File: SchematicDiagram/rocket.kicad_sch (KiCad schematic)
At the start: 5 parts, among them SW1 SW_Push, U1 ESP32-DevKitC

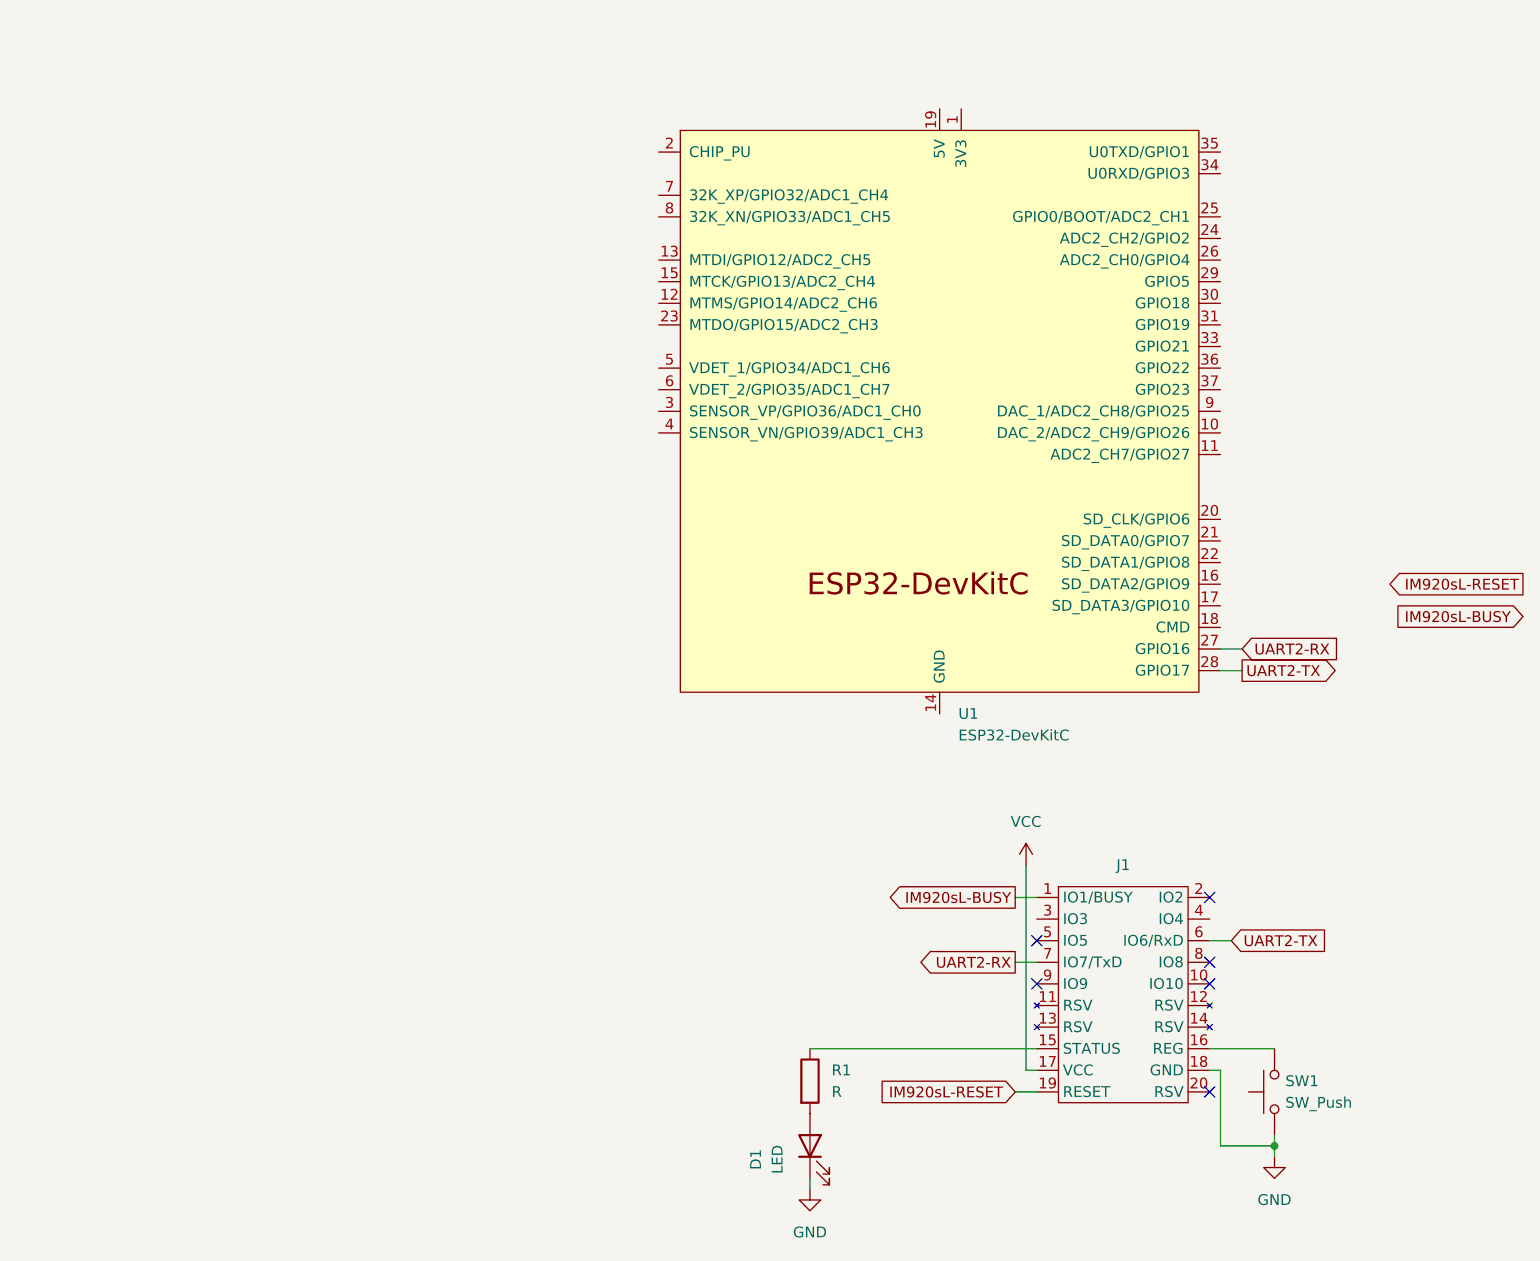
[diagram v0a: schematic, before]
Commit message: add symbole of Regulator Linear
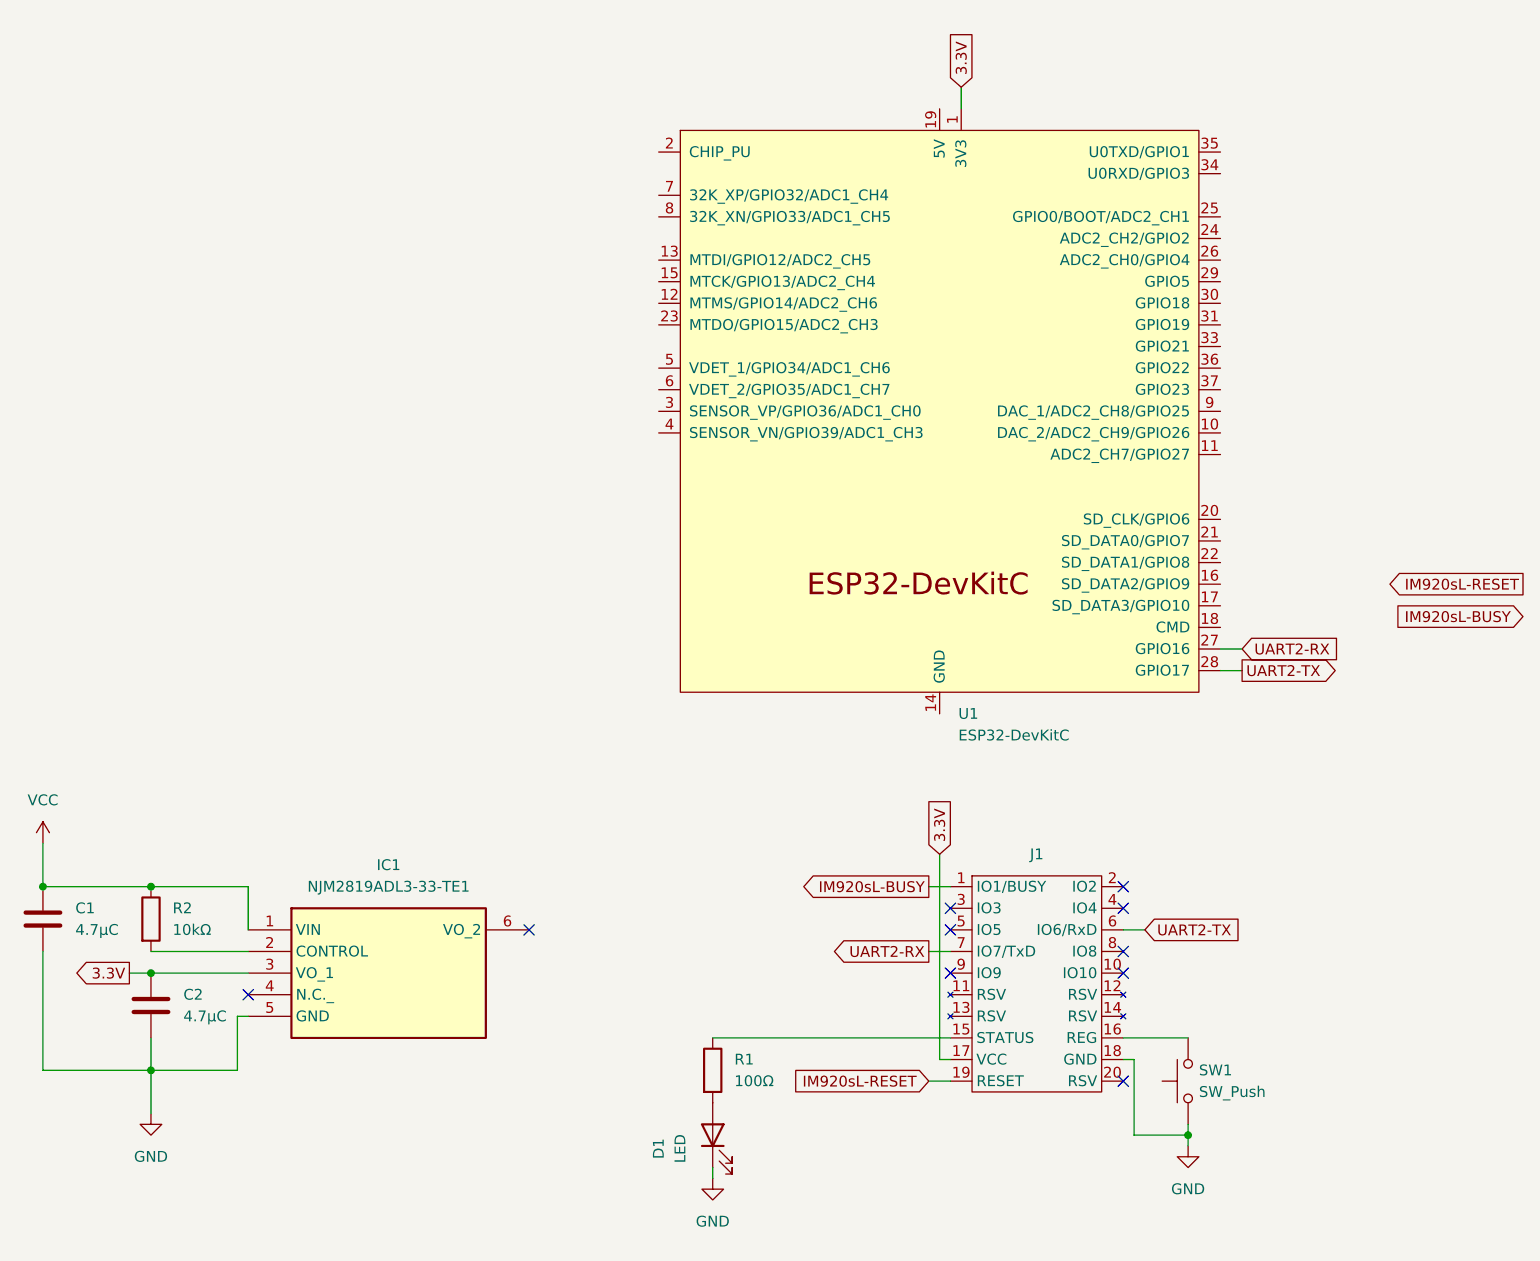
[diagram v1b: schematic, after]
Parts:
- added C1, C2: 4.7μC, symbol Device:C
- added IC1: NJM2819ADL3-33-TE1, NJM2819ADL333TE1, symbol NJM2819ADL3-33-TE1:NJM2819ADL3-33-TE1
- added R2: 10kΩ, symbol Device:R
- R1: value R -> 100Ω
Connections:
- net GND: now also C1.1, C2.1, IC1.5 (GND)
- net VCC: now also C1.2, IC1.1 (VIN), R2.1; no longer J1.17 (VCC)
- net 3.3V: now reaches U1.1 (3V3)
- net 3.3V: now also J1.17 (VCC), C2.2, IC1.3 (VO_1)
- new net: IC1.2 (CONTROL), R2.2
- no-connect marks 6 -> 10
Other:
- moved on the sheet: D1, J1, R1, SW1

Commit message: self voltage manegment
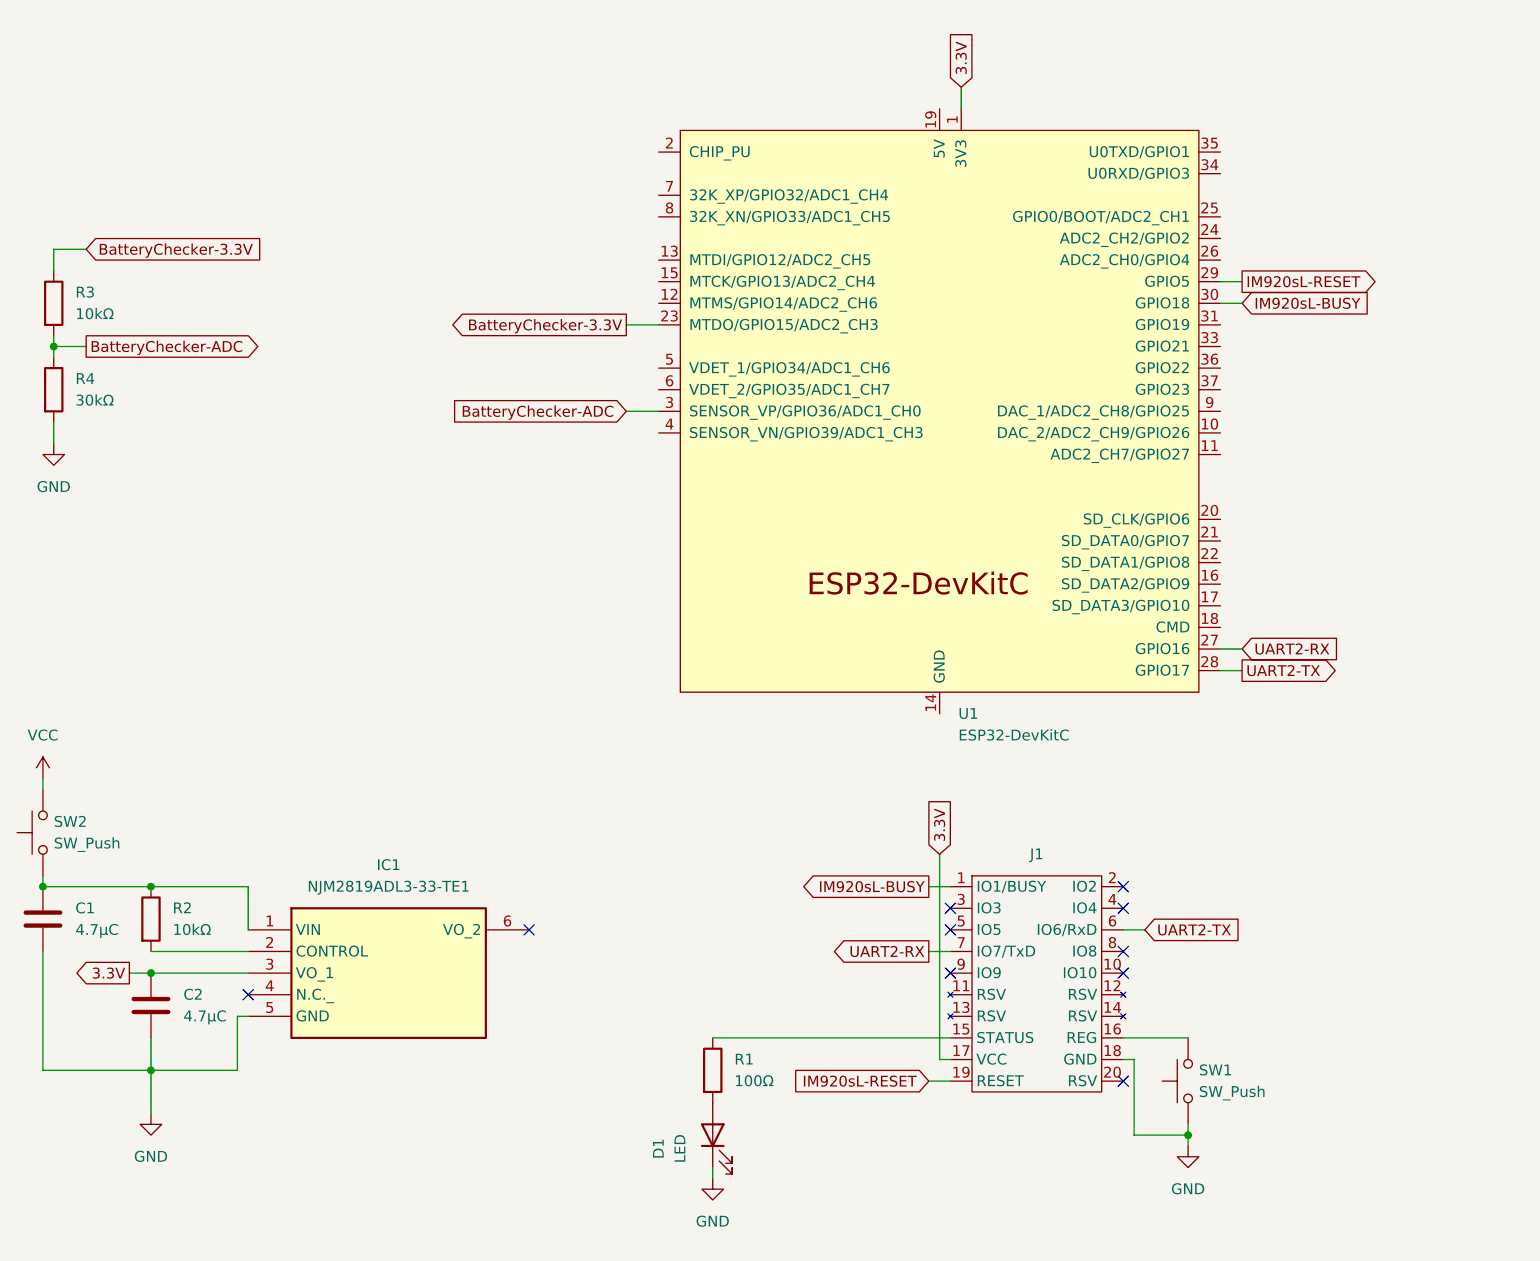
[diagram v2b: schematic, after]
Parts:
- added R3: 10kΩ, symbol Device:R
- added R4: 30kΩ, symbol Device:R
- added SW2: SW_Push, symbol Switch:SW_Push
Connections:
- net GND: now also R4.2
- net IM920sL-BUSY: now also U1.30 (GPIO18)
- net IM920sL-RESET: now also U1.29 (GPIO5)
- net VCC: now also SW2.2; no longer C1.2, IC1.1 (VIN), R2.1
- net BatteryChecker-3.3V: now reaches U1.23 (MTDO/GPIO15/ADC2_CH3)
- net BatteryChecker-3.3V: now also R3.1
- net BatteryChecker-ADC: now reaches U1.3 (SENSOR_VP/GPIO36/ADC1_CH0)
- net BatteryChecker-ADC: now also R3.2, R4.1
- new net: C1.2, IC1.1 (VIN), R2.1, SW2.1
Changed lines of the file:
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@@
   (junction (at 120.65 120.65) (diameter 0) (color 0 0 0 0)
+  )
+  (junction (at 109.22 57.15) (diameter 0) (color 0 0 0 0)
   )
   (junction (at 120.65 130.81) (diameter 0) (color 0 0 0 0)
@@
     (stroke (width 0) (type default))
   )
+  (wire (pts (xy 109.22 68.58) (xy 109.22 66.04))
+    (stroke (width 0) (type default))
+  )
+  (wire (pts (xy 176.53 54.61) (xy 180.34 54.61))
+    (stroke (width 0) (type default))
+  )
   (wire (pts (xy 236.22 149.86) (xy 242.57 149.86))
     (stroke (width 0) (type default))
@@
     (stroke (width 0) (type default))
   )
+  (wire (pts (xy 248.92 52.07) (xy 246.38 52.07))
+    (stroke (width 0) (type default))
+  )
   (wire (pts (xy 118.11 130.81) (xy 120.65 130.81))
     (stroke (width 0) (type default))
   )
+  (wire (pts (xy 107.95 109.22) (xy 107.95 107.95))
+    (stroke (width 0) (type default))
+  )
   (wire (pts (xy 212.09 143.51) (xy 214.63 143.51))
     (stroke (width 0) (type default))
@@
     (stroke (width 0) (type default))
   )
+  (wire (pts (xy 107.95 119.38) (xy 107.95 120.65))
+    (stroke (width 0) (type default))
+  )
   (wire (pts (xy 130.81 142.24) (xy 120.65 142.24))
     (stroke (width 0) (type default))
@@
     (stroke (width 0) (type default))
   )
-  (wire (pts (xy 107.95 115.57) (xy 107.95 120.65))
+  (wire (pts (xy 109.22 57.15) (xy 109.22 58.42))
+    (stroke (width 0) (type default))
+  )
+  (wire (pts (xy 248.92 49.53) (xy 246.38 49.53))
     (stroke (width 0) (type default))
   )
@@
     (stroke (width 0) (type default))
   )
+  (wire (pts (xy 109.22 45.72) (xy 113.03 45.72))
+    (stroke (width 0) (type default))
+  )
+  (wire (pts (xy 109.22 57.15) (xy 113.03 57.15))
+    (stroke (width 0) (type default))
+  )
   (wire (pts (xy 236.22 140.97) (xy 236.22 149.86))
     (stroke (width 0) (type default))
@@
     (stroke (width 0) (type default))
   )
+  (wire (pts (xy 109.22 48.26) (xy 109.22 45.72))
+    (stroke (width 0) (type default))
+  )
   (wire (pts (xy 107.95 142.24) (xy 120.65 142.24))
     (stroke (width 0) (type default))
@@
     (stroke (width 0) (type default))
   )
+  (wire (pts (xy 176.53 64.77) (xy 180.34 64.77))
+    (stroke (width 0) (type default))
+  )
+  (wire (pts (xy 109.22 55.88) (xy 109.22 57.15))
+    (stroke (width 0) (type default))
+  )
   (wire (pts (xy 132.08 120.65) (xy 120.65 120.65))
     (stroke (width 0) (type default))
@@
     )
   )
+  (global_label "BatteryChecker-3.3V" (shape input) (at 113.03 45.72 0) (fields_autoplaced)
+    (effects (font (size 1.27 1.27)) (justify left))
+    (property "Intersheetrefs" "${INTERSHEET_REFS}" (at 135.9119 45.72 0)
+      (effects (font (size 1.27 1.27)) (justify left) hide)
+    )
+  )
   (global_label "UART2-TX" (shape input) (at 237.49 125.73 0) (fields_autoplaced)
     (effects (font (size 1.27 1.27)) (justify left))
@@
     )
   )
-  (global_label "IM920sL-BUSY" (shape input) (at 281.94 88.9 180) (fields_autoplaced)
-    (effects (font (size 1.27 1.27)) (justify right))
-    (property "Intersheetrefs" "${INTERSHEET_REFS}" (at 264.7429 88.9 0)
-      (effects (font (size 1.27 1.27)) (justify right) hide)
+  (global_label "BatteryChecker-ADC" (shape input) (at 176.53 64.77 180) (fields_autoplaced)
+    (effects (font (size 1.27 1.27)) (justify right))
+    (property "Intersheetrefs" "${INTERSHEET_REFS}" (at 154.1319 64.77 0)
+      (effects (font (size 1.27 1.27)) (justify right) hide)
+    )
+  )
+  (global_label "IM920sL-BUSY" (shape input) (at 248.92 52.07 0) (fields_autoplaced)
+    (effects (font (size 1.27 1.27)) (justify left))
+    (property "Intersheetrefs" "${INTERSHEET_REFS}" (at 266.1171 52.07 0)
+      (effects (font (size 1.27 1.27)) (justify left) hide)
     )
   )
@@
     )
   )
+  (global_label "BatteryChecker-3.3V" (shape output) (at 176.53 54.61 180) (fields_autoplaced)
+    (effects (font (size 1.27 1.27)) (justify right))
+    (property "Intersheetrefs" "${INTERSHEET_REFS}" (at 153.6481 54.61 0)
+      (effects (font (size 1.27 1.27)) (justify right) hide)
+    )
+  )
   (global_label "UART2-RX" (shape input) (at 248.92 92.71 0) (fields_autoplaced)
     (effects (font (size 1.27 1.27)) (justify left))
@@
     )
   )
-  (global_label "IM920sL-RESET" (shape output) (at 281.94 85.09 180) (fields_autoplaced)
-    (effects (font (size 1.27 1.27)) (justify right))
-    (property "Intersheetrefs" "${INTERSHEET_REFS}" (at 263.8964 85.09 0)
-      (effects (font (size 1.27 1.27)) (justify right) hide)
+  (global_label "BatteryChecker-ADC" (shape output) (at 113.03 57.15 0) (fields_autoplaced)
+    (effects (font (size 1.27 1.27)) (justify left))
+    (property "Intersheetrefs" "${INTERSHEET_REFS}" (at 135.4281 57.15 0)
+      (effects (font (size 1.27 1.27)) (justify left) hide)
+    )
+  )
+  (global_label "IM920sL-RESET" (shape output) (at 248.92 49.53 0) (fields_autoplaced)
+    (effects (font (size 1.27 1.27)) (justify left))
+    (property "Intersheetrefs" "${INTERSHEET_REFS}" (at 266.9636 49.53 0)
+      (effects (font (size 1.27 1.27)) (justify left) hide)
     )
   )
@@
     )
   )
-  (symbol (lib_id "power:VCC") (at 107.95 115.57 0) (unit 1)
-    (in_bom yes) (on_board yes) (dnp no) (fields_autoplaced)
-    (property "Reference" "#PWR01" (at 107.95 119.38 0)
-      (effects (font (size 1.27 1.27)) hide)
-    )
-    (property "Value" "VCC" (at 107.95 110.49 0)
+  (symbol (lib_id "Device:R") (at 109.22 62.23 0) (unit 1)
+    (in_bom yes) (on_board yes) (dnp no) (fields_autoplaced)
+    (property "Reference" "R4" (at 111.76 60.96 0)
+      (effects (font (size 1.27 1.27)) (justify left))
+    )
+    (property "Value" "30kΩ" (at 111.76 63.5 0)
+      (effects (font (size 1.27 1.27)) (justify left))
+    )
+    (property "Footprint" "" (at 107.442 62.23 90)
+      (effects (font (size 1.27 1.27)) hide)
+    )
+    (property "Datasheet" "~" (at 109.22 62.23 0)
+      (effects (font (size 1.27 1.27)) hide)
+    )
+    (pin "1")
+    (pin "2")
+    (instances
+      (project "rocket"
+        (path "/c0bf920c-eb11-4344-a4ed-62aace3ca89e"
+          (reference "R4") (unit 1)
+        )
+      )
+    )
+  )
+  (symbol (lib_id "power:VCC") (at 107.95 107.95 0) (unit 1)
+    (in_bom yes) (on_board yes) (dnp no) (fields_autoplaced)
+    (property "Reference" "#PWR01" (at 107.95 111.76 0)
+      (effects (font (size 1.27 1.27)) hide)
+    )
+    (property "Value" "VCC" (at 107.95 102.87 0)
       (effects (font (size 1.27 1.27)))
     )
-    (property "Footprint" "" (at 107.95 115.57 0)
-      (effects (font (size 1.27 1.27)) hide)
-    )
-    (property "Datasheet" "" (at 107.95 115.57 0)
+    (property "Footprint" "" (at 107.95 107.95 0)
+      (effects (font (size 1.27 1.27)) hide)
+    )
+    (property "Datasheet" "" (at 107.95 107.95 0)
       (effects (font (size 1.27 1.27)) hide)
     )
@@
     )
   )
+  (symbol (lib_name "GND_2") (lib_id "power:GND") (at 109.22 68.58 0) (unit 1)
+    (in_bom yes) (on_board yes) (dnp no) (fields_autoplaced)
+    (property "Reference" "#PWR05" (at 109.22 74.93 0)
+      (effects (font (size 1.27 1.27)) hide)
+    )
+    (property "Value" "GND" (at 109.22 73.66 0)
+      (effects (font (size 1.27 1.27)))
+    )
+    (property "Footprint" "" (at 109.22 68.58 0)
+      (effects (font (size 1.27 1.27)) hide)
+    )
+    (property "Datasheet" "" (at 109.22 68.58 0)
+      (effects (font (size 1.27 1.27)) hide)
+    )
+    (pin "1")
+    (instances
+      (project "rocket"
+        (path "/c0bf920c-eb11-4344-a4ed-62aace3ca89e"
+          (reference "#PWR05") (unit 1)
+        )
+      )
+    )
+  )
+  (symbol (lib_id "Switch:SW_Push") (at 107.95 114.3 90) (unit 1)
+    (in_bom yes) (on_board yes) (dnp no) (fields_autoplaced)
+    (property "Reference" "SW2" (at 109.22 113.03 90)
+      (effects (font (size 1.27 1.27)) (justify right))
+    )
+    (property "Value" "SW_Push" (at 109.22 115.57 90)
+      (effects (font (size 1.27 1.27)) (justify right))
+    )
+    (property "Footprint" "" (at 102.87 114.3 0)
+      (effects (font (size 1.27 1.27)) hide)
+    )
+    (property "Datasheet" "~" (at 102.87 114.3 0)
+      (effects (font (size 1.27 1.27)) hide)
+    )
+    (pin "2")
+    (pin "1")
+    (instances
+      (project "rocket"
+        (path "/c0bf920c-eb11-4344-a4ed-62aace3ca89e"
+          (reference "SW2") (unit 1)
+        )
+      )
+    )
+  )
   (symbol (lib_id "Switch:SW_Push") (at 242.57 143.51 90) (unit 1)
     (in_bom yes) (on_board yes) (dnp no) (fields_autoplaced)
@@
         )
       )
+    )
+  )
+  (symbol (lib_id "Device:R") (at 109.22 52.07 0) (unit 1)
+    (in_bom yes) (on_board yes) (dnp no) (fields_autoplaced)
+    (property "Reference" "R3" (at 111.76 50.8 0)
+      (effects (font (size 1.27 1.27)) (justify left))
+    )
+    (property "Value" "10kΩ" (at 111.76 53.34 0)
+      (effects (font (size 1.27 1.27)) (justify left))
+    )
+    (property "Footprint" "" (at 107.442 52.07 90)
+      (effects (font (size 1.27 1.27)) hide)
+    )
+    (property "Datasheet" "~" (at 109.22 52.07 0)
+      (effects (font (size 1.27 1.27)) hide)
+    )
+    (pin "1")
+    (pin "2")
+    (instances
+      (project "rocket"
+        (path "/c0bf920c-eb11-4344-a4ed-62aace3ca89e"
+          (reference "R3") (unit 1)
+        )
+      )
